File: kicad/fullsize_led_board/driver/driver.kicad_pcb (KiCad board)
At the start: 2 copper layers, 0 parts

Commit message: fullsize led board: driver pcb outline and connectors placed
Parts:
- added C1: 100nF, Capacitor_THT:C_Disc_D4.7mm_W2.5mm_P5.00mm, F.Cu at (163.9, 71.9)
- added C2: 100nF, Capacitor_THT:C_Disc_D4.7mm_W2.5mm_P5.00mm, F.Cu at (163.9, 75.9)
- added C3: 100nF, Capacitor_THT:C_Disc_D4.7mm_W2.5mm_P5.00mm, F.Cu at (163.9, 80.0)
- added C4: 100nF, Capacitor_THT:C_Disc_D4.7mm_W2.5mm_P5.00mm, F.Cu at (163.9, 84.0)
- added C5: 100nF, Capacitor_THT:C_Disc_D4.7mm_W2.5mm_P5.00mm, F.Cu at (163.9, 88.1)
- added C6: 100nF, Capacitor_THT:C_Disc_D4.7mm_W2.5mm_P5.00mm, F.Cu at (163.9, 92.1)
- added C7: 100nF, Capacitor_THT:C_Disc_D4.7mm_W2.5mm_P5.00mm, F.Cu at (163.9, 96.2)
- added C8: 100nF, Capacitor_THT:C_Disc_D4.7mm_W2.5mm_P5.00mm, F.Cu at (163.9, 100.2)
- added J1: ~, Connector_PinHeader_2.54mm:PinHeader_1x02_P2.54mm_Horizontal, F.Cu at (249.9, 123.7)
- added J2: ~, Connector_BarrelJack:BarrelJack_Horizontal, F.Cu at (246.0, 137.0)
- added J3: ~, Connector_PinHeader_2.54mm:PinHeader_2x05_P2.54mm_Horizontal, F.Cu at (247.3, 108.5)
- added J4: Anodes Header, Connector_PinSocket_2.54mm:PinSocket_1x24_P2.54mm_Vertical, F.Cu at (257.0, 40.0)
- added J5: Cathodes Header, Connector_PinSocket_2.54mm:PinSocket_1x32_P2.54mm_Vertical, F.Cu at (103.9, 157.0)
- added Q1: SQ2351CES, Package_TO_SOT_SMD:SOT-23-3, F.Cu at (173.1, 72.2)
- added Q10: SQ2351CES, Package_TO_SOT_SMD:SOT-23-3, F.Cu at (178.2, 81.5)
- added Q11: SQ2351CES, Package_TO_SOT_SMD:SOT-23-3, F.Cu at (178.2, 86.1)
- added Q12: SQ2351CES, Package_TO_SOT_SMD:SOT-23-3, F.Cu at (178.2, 90.8)
- added Q13: SQ2351CES, Package_TO_SOT_SMD:SOT-23-3, F.Cu at (178.2, 95.4)
- added Q14: SQ2351CES, Package_TO_SOT_SMD:SOT-23-3, F.Cu at (178.2, 100.0)
- added Q15: SQ2351CES, Package_TO_SOT_SMD:SOT-23-3, F.Cu at (183.4, 72.2)
- added Q16: SQ2351CES, Package_TO_SOT_SMD:SOT-23-3, F.Cu at (183.4, 76.9)
- added Q17: SQ2351CES, Package_TO_SOT_SMD:SOT-23-3, F.Cu at (183.4, 81.5)
- added Q18: SQ2351CES, Package_TO_SOT_SMD:SOT-23-3, F.Cu at (183.4, 86.1)
- added Q19: SQ2351CES, Package_TO_SOT_SMD:SOT-23-3, F.Cu at (183.4, 90.8)
- added Q2: SQ2351CES, Package_TO_SOT_SMD:SOT-23-3, F.Cu at (173.1, 76.9)
- added Q20: SQ2351CES, Package_TO_SOT_SMD:SOT-23-3, F.Cu at (183.4, 95.4)
- added Q21: SQ2351CES, Package_TO_SOT_SMD:SOT-23-3, F.Cu at (183.4, 100.0)
- added Q22: SQ2351CES, Package_TO_SOT_SMD:SOT-23-3, F.Cu at (188.5, 72.2)
- added Q23: SQ2351CES, Package_TO_SOT_SMD:SOT-23-3, F.Cu at (188.5, 76.9)
- added Q24: SQ2351CES, Package_TO_SOT_SMD:SOT-23-3, F.Cu at (188.5, 81.5)
- added Q3: SQ2351CES, Package_TO_SOT_SMD:SOT-23-3, F.Cu at (173.1, 81.5)
- added Q4: SQ2351CES, Package_TO_SOT_SMD:SOT-23-3, F.Cu at (173.1, 86.1)
- added Q5: SQ2351CES, Package_TO_SOT_SMD:SOT-23-3, F.Cu at (173.1, 90.8)
- added Q6: SQ2351CES, Package_TO_SOT_SMD:SOT-23-3, F.Cu at (173.1, 95.4)
- added Q7: SQ2351CES, Package_TO_SOT_SMD:SOT-23-3, F.Cu at (173.1, 100.0)
- added Q8: SQ2351CES, Package_TO_SOT_SMD:SOT-23-3, F.Cu at (178.2, 72.2)
- added Q9: SQ2351CES, Package_TO_SOT_SMD:SOT-23-3, F.Cu at (178.2, 76.9)
- added R1: R, Resistor_THT:R_Axial_DIN0207_L6.3mm_D2.5mm_P7.62mm_Horizontal, F.Cu at (110.1, 71.9)
- added R10: 150R, Resistor_THT:R_Axial_DIN0207_L6.3mm_D2.5mm_P7.62mm_Horizontal, F.Cu at (110.1, 108.3)
- added R11: R, Resistor_THT:R_Axial_DIN0207_L6.3mm_D2.5mm_P7.62mm_Horizontal, F.Cu at (110.1, 112.4)
- added R12: 150R, Resistor_THT:R_Axial_DIN0207_L6.3mm_D2.5mm_P7.62mm_Horizontal, F.Cu at (120.8, 71.9)
- added R13: R, Resistor_THT:R_Axial_DIN0207_L6.3mm_D2.5mm_P7.62mm_Horizontal, F.Cu at (120.8, 75.9)
- added R14: 150R, Resistor_THT:R_Axial_DIN0207_L6.3mm_D2.5mm_P7.62mm_Horizontal, F.Cu at (120.8, 80.0)
- added R15: R, Resistor_THT:R_Axial_DIN0207_L6.3mm_D2.5mm_P7.62mm_Horizontal, F.Cu at (120.8, 84.0)
- added R16: 150R, Resistor_THT:R_Axial_DIN0207_L6.3mm_D2.5mm_P7.62mm_Horizontal, F.Cu at (120.8, 88.1)
- added R17: R, Resistor_THT:R_Axial_DIN0207_L6.3mm_D2.5mm_P7.62mm_Horizontal, F.Cu at (120.8, 92.1)
- added R18: 150R, Resistor_THT:R_Axial_DIN0207_L6.3mm_D2.5mm_P7.62mm_Horizontal, F.Cu at (120.8, 96.2)
- added R19: R, Resistor_THT:R_Axial_DIN0207_L6.3mm_D2.5mm_P7.62mm_Horizontal, F.Cu at (120.8, 100.2)
- added R2: R, Resistor_THT:R_Axial_DIN0207_L6.3mm_D2.5mm_P7.62mm_Horizontal, F.Cu at (110.1, 75.9)
- added R20: 150R, Resistor_THT:R_Axial_DIN0207_L6.3mm_D2.5mm_P7.62mm_Horizontal, F.Cu at (120.8, 104.3)
- added R21: R, Resistor_THT:R_Axial_DIN0207_L6.3mm_D2.5mm_P7.62mm_Horizontal, F.Cu at (120.8, 108.3)
- added R22: 150R, Resistor_THT:R_Axial_DIN0207_L6.3mm_D2.5mm_P7.62mm_Horizontal, F.Cu at (120.8, 112.4)
- added R23: R, Resistor_THT:R_Axial_DIN0207_L6.3mm_D2.5mm_P7.62mm_Horizontal, F.Cu at (131.6, 71.9)
- added R24: 150R, Resistor_THT:R_Axial_DIN0207_L6.3mm_D2.5mm_P7.62mm_Horizontal, F.Cu at (131.6, 75.9)
- added R25: R, Resistor_THT:R_Axial_DIN0207_L6.3mm_D2.5mm_P7.62mm_Horizontal, F.Cu at (131.6, 80.0)
- added R26: 150R, Resistor_THT:R_Axial_DIN0207_L6.3mm_D2.5mm_P7.62mm_Horizontal, F.Cu at (131.6, 84.0)
- added R27: R, Resistor_THT:R_Axial_DIN0207_L6.3mm_D2.5mm_P7.62mm_Horizontal, F.Cu at (131.6, 88.1)
- added R28: 150R, Resistor_THT:R_Axial_DIN0207_L6.3mm_D2.5mm_P7.62mm_Horizontal, F.Cu at (131.6, 92.1)
- added R29: R, Resistor_THT:R_Axial_DIN0207_L6.3mm_D2.5mm_P7.62mm_Horizontal, F.Cu at (131.6, 96.2)
- added R3: R, Resistor_THT:R_Axial_DIN0207_L6.3mm_D2.5mm_P7.62mm_Horizontal, F.Cu at (110.1, 80.0)
- added R30: 150R, Resistor_THT:R_Axial_DIN0207_L6.3mm_D2.5mm_P7.62mm_Horizontal, F.Cu at (131.6, 100.2)
- added R31: R, Resistor_THT:R_Axial_DIN0207_L6.3mm_D2.5mm_P7.62mm_Horizontal, F.Cu at (131.6, 104.3)
- added R32: 150R, Resistor_THT:R_Axial_DIN0207_L6.3mm_D2.5mm_P7.62mm_Horizontal, F.Cu at (131.6, 108.3)
- added R33: R, Resistor_THT:R_Axial_DIN0207_L6.3mm_D2.5mm_P7.62mm_Horizontal, F.Cu at (131.6, 112.4)
- added R34: 150R, Resistor_THT:R_Axial_DIN0207_L6.3mm_D2.5mm_P7.62mm_Horizontal, F.Cu at (142.4, 71.9)
- added R35: R, Resistor_THT:R_Axial_DIN0207_L6.3mm_D2.5mm_P7.62mm_Horizontal, F.Cu at (142.4, 75.9)
- added R36: 150R, Resistor_THT:R_Axial_DIN0207_L6.3mm_D2.5mm_P7.62mm_Horizontal, F.Cu at (142.4, 80.0)
- added R37: R, Resistor_THT:R_Axial_DIN0207_L6.3mm_D2.5mm_P7.62mm_Horizontal, F.Cu at (142.4, 84.0)
- added R38: 150R, Resistor_THT:R_Axial_DIN0207_L6.3mm_D2.5mm_P7.62mm_Horizontal, F.Cu at (142.4, 88.1)
- added R39: R, Resistor_THT:R_Axial_DIN0207_L6.3mm_D2.5mm_P7.62mm_Horizontal, F.Cu at (142.4, 92.1)
- added R4: R, Resistor_THT:R_Axial_DIN0207_L6.3mm_D2.5mm_P7.62mm_Horizontal, F.Cu at (110.1, 84.0)
- added R40: 150R, Resistor_THT:R_Axial_DIN0207_L6.3mm_D2.5mm_P7.62mm_Horizontal, F.Cu at (142.4, 96.2)
- added R41: R, Resistor_THT:R_Axial_DIN0207_L6.3mm_D2.5mm_P7.62mm_Horizontal, F.Cu at (142.4, 100.2)
- added R42: 150R, Resistor_THT:R_Axial_DIN0207_L6.3mm_D2.5mm_P7.62mm_Horizontal, F.Cu at (142.4, 104.3)
- added R43: R, Resistor_THT:R_Axial_DIN0207_L6.3mm_D2.5mm_P7.62mm_Horizontal, F.Cu at (142.4, 108.3)
- added R44: 150R, Resistor_THT:R_Axial_DIN0207_L6.3mm_D2.5mm_P7.62mm_Horizontal, F.Cu at (142.4, 112.4)
- added R45: R, Resistor_THT:R_Axial_DIN0207_L6.3mm_D2.5mm_P7.62mm_Horizontal, F.Cu at (153.1, 71.9)
- added R46: 150R, Resistor_THT:R_Axial_DIN0207_L6.3mm_D2.5mm_P7.62mm_Horizontal, F.Cu at (153.1, 75.9)
- added R47: R, Resistor_THT:R_Axial_DIN0207_L6.3mm_D2.5mm_P7.62mm_Horizontal, F.Cu at (153.1, 80.0)
- added R48: 150R, Resistor_THT:R_Axial_DIN0207_L6.3mm_D2.5mm_P7.62mm_Horizontal, F.Cu at (153.1, 84.0)
- added R49: R, Resistor_THT:R_Axial_DIN0207_L6.3mm_D2.5mm_P7.62mm_Horizontal, F.Cu at (153.1, 88.1)
- added R5: R, Resistor_THT:R_Axial_DIN0207_L6.3mm_D2.5mm_P7.62mm_Horizontal, F.Cu at (110.1, 88.1)
- added R50: 150R, Resistor_THT:R_Axial_DIN0207_L6.3mm_D2.5mm_P7.62mm_Horizontal, F.Cu at (153.1, 92.1)
- added R51: R, Resistor_THT:R_Axial_DIN0207_L6.3mm_D2.5mm_P7.62mm_Horizontal, F.Cu at (153.1, 96.2)
- added R52: 150R, Resistor_THT:R_Axial_DIN0207_L6.3mm_D2.5mm_P7.62mm_Horizontal, F.Cu at (153.1, 100.2)
- added R53: R, Resistor_THT:R_Axial_DIN0207_L6.3mm_D2.5mm_P7.62mm_Horizontal, F.Cu at (153.1, 104.3)
- added R54: 150R, Resistor_THT:R_Axial_DIN0207_L6.3mm_D2.5mm_P7.62mm_Horizontal, F.Cu at (153.1, 108.3)
- added R55: R, Resistor_THT:R_Axial_DIN0207_L6.3mm_D2.5mm_P7.62mm_Horizontal, F.Cu at (103.9, 149.5)
- added R56: R, Resistor_THT:R_Axial_DIN0207_L6.3mm_D2.5mm_P7.62mm_Horizontal, F.Cu at (106.9, 149.5)
- added R57: R, Resistor_THT:R_Axial_DIN0207_L6.3mm_D2.5mm_P7.62mm_Horizontal, F.Cu at (109.9, 149.5)
- added R58: R, Resistor_THT:R_Axial_DIN0207_L6.3mm_D2.5mm_P7.62mm_Horizontal, F.Cu at (112.9, 149.5)
- added R59: R, Resistor_THT:R_Axial_DIN0207_L6.3mm_D2.5mm_P7.62mm_Horizontal, F.Cu at (115.9, 149.5)
- added R6: R, Resistor_THT:R_Axial_DIN0207_L6.3mm_D2.5mm_P7.62mm_Horizontal, F.Cu at (110.1, 92.1)
- added R60: R, Resistor_THT:R_Axial_DIN0207_L6.3mm_D2.5mm_P7.62mm_Horizontal, F.Cu at (118.9, 149.5)
- added R61: R, Resistor_THT:R_Axial_DIN0207_L6.3mm_D2.5mm_P7.62mm_Horizontal, F.Cu at (121.9, 149.5)
- added R62: R, Resistor_THT:R_Axial_DIN0207_L6.3mm_D2.5mm_P7.62mm_Horizontal, F.Cu at (124.9, 149.5)
- added R63: R, Resistor_THT:R_Axial_DIN0207_L6.3mm_D2.5mm_P7.62mm_Horizontal, F.Cu at (127.9, 149.5)
- added R64: R, Resistor_THT:R_Axial_DIN0207_L6.3mm_D2.5mm_P7.62mm_Horizontal, F.Cu at (130.9, 149.5)
- added R65: R, Resistor_THT:R_Axial_DIN0207_L6.3mm_D2.5mm_P7.62mm_Horizontal, F.Cu at (133.9, 149.5)
- added R66: R, Resistor_THT:R_Axial_DIN0207_L6.3mm_D2.5mm_P7.62mm_Horizontal, F.Cu at (136.9, 149.5)
- added R67: R, Resistor_THT:R_Axial_DIN0207_L6.3mm_D2.5mm_P7.62mm_Horizontal, F.Cu at (139.9, 149.5)
- added R68: R, Resistor_THT:R_Axial_DIN0207_L6.3mm_D2.5mm_P7.62mm_Horizontal, F.Cu at (142.9, 149.5)
- added R69: R, Resistor_THT:R_Axial_DIN0207_L6.3mm_D2.5mm_P7.62mm_Horizontal, F.Cu at (145.9, 149.5)
- added R7: R, Resistor_THT:R_Axial_DIN0207_L6.3mm_D2.5mm_P7.62mm_Horizontal, F.Cu at (110.1, 96.2)
- added R70: R, Resistor_THT:R_Axial_DIN0207_L6.3mm_D2.5mm_P7.62mm_Horizontal, F.Cu at (148.9, 149.5)
- added R71: R, Resistor_THT:R_Axial_DIN0207_L6.3mm_D2.5mm_P7.62mm_Horizontal, F.Cu at (151.9, 149.5)
- added R72: R, Resistor_THT:R_Axial_DIN0207_L6.3mm_D2.5mm_P7.62mm_Horizontal, F.Cu at (154.9, 149.5)
- added R73: R, Resistor_THT:R_Axial_DIN0207_L6.3mm_D2.5mm_P7.62mm_Horizontal, F.Cu at (157.9, 149.5)
- added R74: R, Resistor_THT:R_Axial_DIN0207_L6.3mm_D2.5mm_P7.62mm_Horizontal, F.Cu at (160.9, 149.5)
- added R75: R, Resistor_THT:R_Axial_DIN0207_L6.3mm_D2.5mm_P7.62mm_Horizontal, F.Cu at (163.9, 149.5)
- added R76: R, Resistor_THT:R_Axial_DIN0207_L6.3mm_D2.5mm_P7.62mm_Horizontal, F.Cu at (166.9, 149.5)
- added R77: R, Resistor_THT:R_Axial_DIN0207_L6.3mm_D2.5mm_P7.62mm_Horizontal, F.Cu at (169.9, 149.5)
- added R78: R, Resistor_THT:R_Axial_DIN0207_L6.3mm_D2.5mm_P7.62mm_Horizontal, F.Cu at (172.9, 149.5)
- added R79: R, Resistor_THT:R_Axial_DIN0207_L6.3mm_D2.5mm_P7.62mm_Horizontal, F.Cu at (175.9, 149.5)
- added R8: 150R, Resistor_THT:R_Axial_DIN0207_L6.3mm_D2.5mm_P7.62mm_Horizontal, F.Cu at (110.1, 100.2)
- added R80: R, Resistor_THT:R_Axial_DIN0207_L6.3mm_D2.5mm_P7.62mm_Horizontal, F.Cu at (178.9, 149.5)
- added R81: R, Resistor_THT:R_Axial_DIN0207_L6.3mm_D2.5mm_P7.62mm_Horizontal, F.Cu at (181.9, 149.5)
- added R82: R, Resistor_THT:R_Axial_DIN0207_L6.3mm_D2.5mm_P7.62mm_Horizontal, F.Cu at (184.9, 149.5)
- added R83: R, Resistor_THT:R_Axial_DIN0207_L6.3mm_D2.5mm_P7.62mm_Horizontal, F.Cu at (187.9, 149.5)
- added R84: R, Resistor_THT:R_Axial_DIN0207_L6.3mm_D2.5mm_P7.62mm_Horizontal, F.Cu at (190.9, 149.5)
- added R85: R, Resistor_THT:R_Axial_DIN0207_L6.3mm_D2.5mm_P7.62mm_Horizontal, F.Cu at (193.9, 149.5)
- added R86: R, Resistor_THT:R_Axial_DIN0207_L6.3mm_D2.5mm_P7.62mm_Horizontal, F.Cu at (196.9, 149.5)
- added R9: R, Resistor_THT:R_Axial_DIN0207_L6.3mm_D2.5mm_P7.62mm_Horizontal, F.Cu at (110.1, 104.3)
- added U1: 74HCT541, Package_DIP:DIP-20_W7.62mm, F.Cu at (110.1, 44.9)
- added U2: 74HCT595, Package_SO:SOIC-16_3.9x9.9mm_P1.27mm, F.Cu at (167.0, 48.7)
- added U3: 74HCT595, Package_SO:SOIC-16_3.9x9.9mm_P1.27mm, F.Cu at (175.4, 48.7)
- added U4: 74HCT595, Package_SO:SOIC-16_3.9x9.9mm_P1.27mm, F.Cu at (183.9, 48.7)
- added U5: TPIC6B595N, Package_DIP:DIP-20_W7.62mm, F.Cu at (121.0, 44.9)
- added U6: TPIC6B595N, Package_DIP:DIP-20_W7.62mm, F.Cu at (131.8, 44.9)
- added U7: TPIC6B595N, Package_DIP:DIP-20_W7.62mm, F.Cu at (142.7, 44.9)
- added U8: TPIC6B595N, Package_DIP:DIP-20_W7.62mm, F.Cu at (153.5, 44.9)
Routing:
- net Net-(J1-Pin_2): track 0.00 -> 6.40 mm
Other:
- board outline added: 163.5 x 127.5 mm
- rule pad_to_mask_clearance: 0 -> 0.038

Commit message: fullsize led board: anode components placed and partially wired
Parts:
- Q10, Q12, Q14, Q16, Q18, Q2, Q20, Q22, Q24, Q4, Q6, Q8, U1, U2, U3, U4: moved to B.Cu
- R1, R11, R13, R15, R17, R19, R2, R21, R23, R25, R27, R29, R3, R31, R33, R35, R37, R39, R4, R41, R43, R45, R47, R49, R5, R51, R53, R6, R7, R9: value R -> 10K
- moved C4 156.0 mm to (313.0, 38.0), turned to -90 degrees
- moved C3 146.7 mm to (304.5, 38.0), turned to -90 degrees
- moved R11 144.3 mm to (235.8, 41.7), turned to 180 degrees
- moved R9 141.8 mm to (235.8, 38.7), turned to 180 degrees
- moved R7 139.5 mm to (235.8, 35.7), turned to 180 degrees
- moved C2 138.6 mm to (295.0, 31.0), turned to -90 degrees
- moved C5 138.5 mm to (25.5, 84.5)
- moved R10 134.7 mm to (225.3, 38.7), turned to 180 degrees
- moved R8 132.1 mm to (225.3, 35.7), turned to 180 degrees
- moved R6 131.6 mm to (232.0, 141.6), turned to 90 degrees
- moved R5 130.4 mm to (229.0, 141.6), turned to 90 degrees
- moved R4 129.5 mm to (226.0, 141.6), turned to 90 degrees
- moved R3 128.7 mm to (223.0, 141.6), turned to 90 degrees
- moved C6 128.6 mm to (35.5, 84.5)
- moved R2 128.1 mm to (220.0, 141.6), turned to 90 degrees
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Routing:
- net +5V: track 0.00 -> 263.0 mm, vias 0 -> 12
- net Net-(Q2-G): track 0.00 -> 21.0 mm, vias 0 -> 1
- net Net-(Q23-G): track 0.00 -> 20.6 mm
- net Net-(Q4-G): track 0.00 -> 20.5 mm, vias 0 -> 1
- net Net-(Q3-G): track 0.00 -> 20.0 mm
- net Net-(Q10-G): track 0.00 -> 19.7 mm, vias 0 -> 1
- net Net-(Q24-G): track 0.00 -> 19.6 mm, vias 0 -> 1
- net Net-(Q5-G): track 0.00 -> 19.5 mm
- net Net-(Q1-G): track 0.00 -> 19.5 mm
- net Net-(Q21-G): track 0.00 -> 19.4 mm
- net Net-(Q6-G): track 0.00 -> 19.3 mm, vias 0 -> 1
- net Net-(Q22-G): track 0.00 -> 19.2 mm, vias 0 -> 1
- net Net-(Q19-G): track 0.00 -> 19.1 mm
- net Net-(Q8-G): track 0.00 -> 19.0 mm, vias 0 -> 1
- net Net-(Q20-G): track 0.00 -> 18.8 mm, vias 0 -> 1
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- added copper zone on B.Cu, net GND

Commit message: fullsize led board: placed buffer and its pullups
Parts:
- C1: moved to B.Cu
- moved C1 162.0 mm to (206.0, 111.5), turned to 0 degrees
- moved C4 127.0 mm to (198.0, 92.0)
- moved C3 112.3 mm to (197.0, 70.5)
- moved C2 94.5 mm to (201.0, 40.5)
- moved R1 16.0 mm to (230.8, 133.5), turned to 180 degrees
- moved R2 12.0 mm to (230.8, 136.5), turned to 180 degrees
- moved R3 8.09 mm to (230.8, 139.5), turned to 180 degrees
- moved R6 6.98 mm to (230.8, 148.5), turned to 180 degrees
- moved R4 4.89 mm to (230.8, 142.5), turned to 180 degrees
- moved U1 4.40 mm to (212.3, 114.6)
- moved R5 4.28 mm to (230.8, 145.5), turned to 180 degrees
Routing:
- net RowData: track 0.00 -> 80.2 mm
- net ShiftRowData: track 0.00 -> 75.7 mm
- net RowStrobe: track 0.00 -> 74.8 mm
- net ShiftRowStrobe: track 0.00 -> 74.1 mm
- net ApplyRowAndStrobe: track 0.00 -> 71.1 mm
- net ~{OutputEnable}: track 0.00 -> 58.0 mm, vias 0 -> 1
- net +5V: track 263.0 -> 298.2 mm

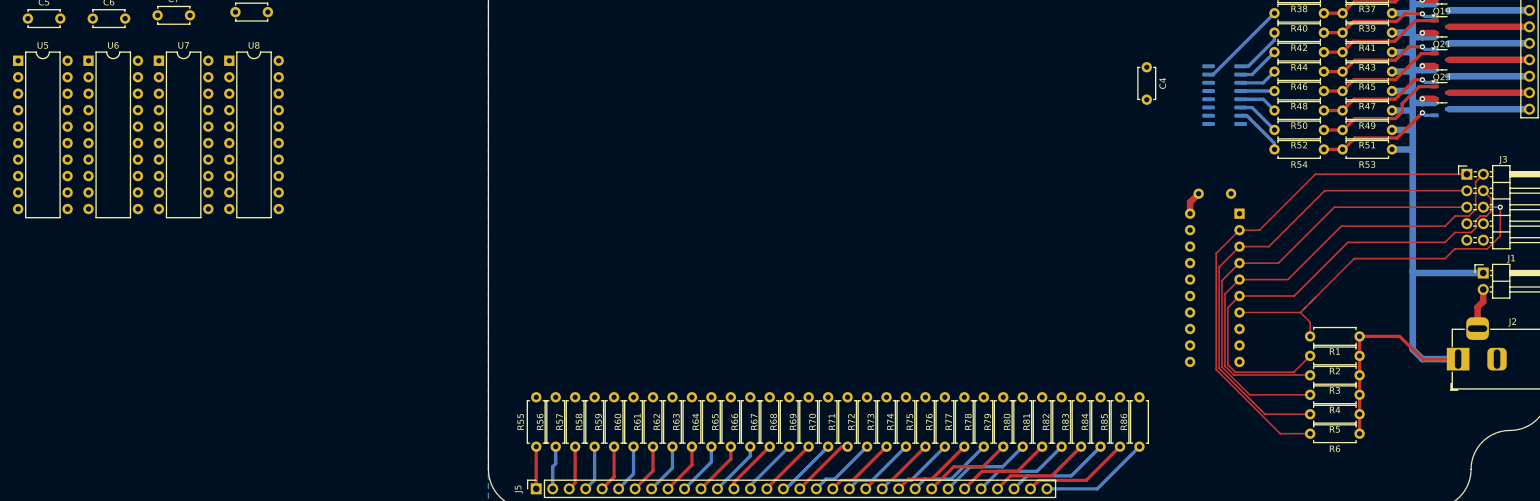
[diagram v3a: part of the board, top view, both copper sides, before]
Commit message: fullsize led board: placed and mostly routed row data shift registers
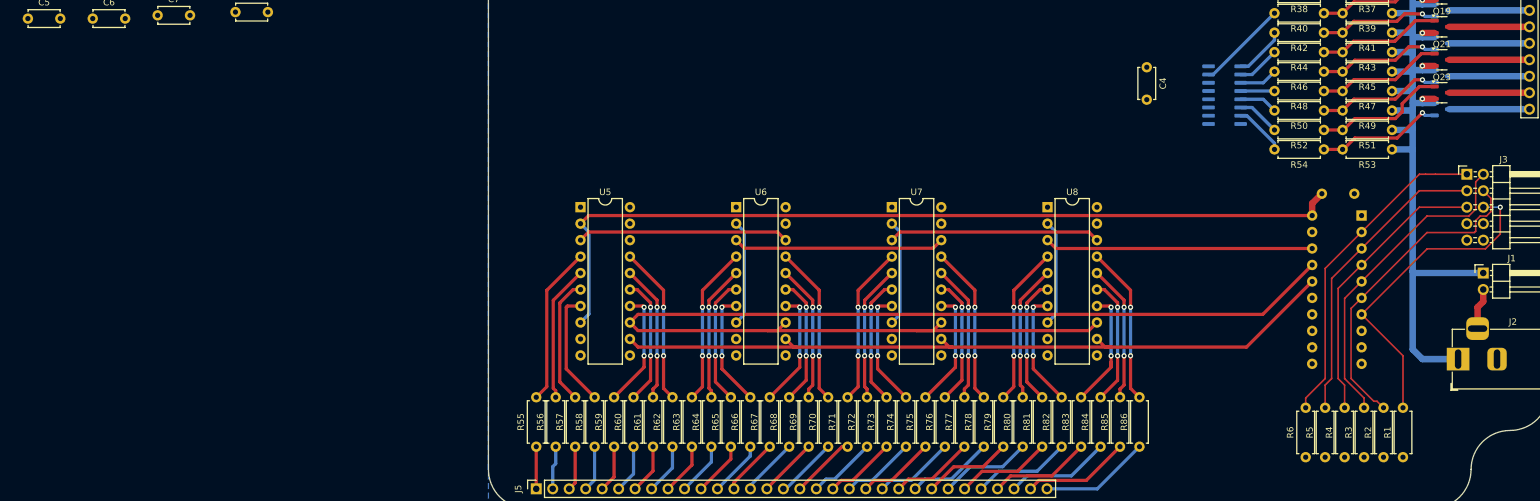
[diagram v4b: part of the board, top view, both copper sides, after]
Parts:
- moved U8 128.2 mm to (182.7, 113.6)
- moved U7 115.2 mm to (158.7, 113.6)
- moved U6 102.4 mm to (134.7, 113.6)
- moved U5 89.6 mm to (110.7, 113.6)
- moved R1 19.8 mm to (237.5, 152.1), turned to 90 degrees
- moved C1 19.0 mm to (225.0, 111.5)
- moved U1 18.8 mm to (231.1, 114.9)
- moved R2 16.0 mm to (234.5, 152.1), turned to 90 degrees
- moved R3 12.6 mm to (231.5, 152.1), turned to 90 degrees
- moved R4 9.89 mm to (228.5, 152.1), turned to 90 degrees
- moved R6 9.06 mm to (222.5, 152.1), turned to 90 degrees
- moved R5 8.49 mm to (225.5, 152.1), turned to 90 degrees
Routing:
- net /ShiftRowData': track 0.00 -> 189.6 mm
- net +5V: track 298.2 -> 445.4 mm
- net /ApplyRowAndStrobe': track 0.00 -> 117.0 mm
- net /RowData': track 0.00 -> 41.7 mm
- net Net-(U7-SER_IN): track 0.00 -> 32.7 mm
- net Net-(U6-SER_IN): track 0.00 -> 32.7 mm
- net Net-(U5-SER_IN): track 0.00 -> 32.7 mm
- net RowData: track 80.2 -> 50.6 mm
- net ShiftRowData: track 75.7 -> 46.8 mm
- net ApplyRowAndStrobe: track 71.1 -> 43.8 mm
- net RowStrobe: track 74.8 -> 49.9 mm
- net /Cathodes8: track 0.00 -> 24.5 mm, vias 0 -> 2
- net /Cathodes0: track 0.00 -> 24.5 mm
- net /Cathodes24: track 0.00 -> 24.5 mm, vias 0 -> 2
- net /Cathodes16: track 0.00 -> 24.5 mm, vias 0 -> 2
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
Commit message: fullsize led board: rearranged high-side resistors to eliminate voltage divier
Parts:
- moved C8 124.3 mm to (179.8, 106.2)
- moved C7 114.8 mm to (158.2, 105.8)
- moved C6 99.9 mm to (133.8, 102.5)
- moved C5 88.3 mm to (112.5, 99.8)
- moved R11 7.62 mm to (228.2, 41.7), turned to 0 degrees
- moved R13 7.62 mm to (228.2, 44.7), turned to 0 degrees
- moved R15 7.62 mm to (228.2, 47.7), turned to 0 degrees
- moved R17 7.62 mm to (228.2, 50.7), turned to 0 degrees
- moved R19 7.62 mm to (228.2, 53.7), turned to 0 degrees
- moved R21 7.62 mm to (228.2, 56.7), turned to 0 degrees
- moved R23 7.62 mm to (228.2, 59.7), turned to 0 degrees
- moved R25 7.62 mm to (228.2, 62.7), turned to 0 degrees
- moved R27 7.62 mm to (228.2, 65.7), turned to 0 degrees
- moved R29 7.62 mm to (228.2, 68.7), turned to 0 degrees
- moved R31 7.62 mm to (228.2, 71.7), turned to 0 degrees
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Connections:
- J3 pad 1: RowData -> ApplyRowAndStrobe
- J3 pad 2: RowStrobe -> ApplyRowAndStrobe
- J3 pad 3: ShiftRowData -> ApplyRowAndStrobe
- J3 pad 6: ~{OutputEnable} -> ApplyRowAndStrobe
- Q17 pad 2: +5V -> unconnected-(Q17-S-Pad2)
- Q17 pad 3: /Anodes16 -> unconnected-(Q17-D-Pad3)
- Q18 pad 2: +5V -> unconnected-(Q18-S-Pad2)
- Q18 pad 3: /Anodes17 -> unconnected-(Q18-D-Pad3)
- Q19 pad 2: +5V -> unconnected-(Q19-S-Pad2)
- Q19 pad 3: /Anodes18 -> unconnected-(Q19-D-Pad3)
- Q20 pad 2: +5V -> unconnected-(Q20-S-Pad2)
- Q20 pad 3: /Anodes19 -> unconnected-(Q20-D-Pad3)
- Q21 pad 2: +5V -> unconnected-(Q21-S-Pad2)
- Q21 pad 3: /Anodes20 -> unconnected-(Q21-D-Pad3)
- Q22 pad 2: +5V -> unconnected-(Q22-S-Pad2)
- Q22 pad 3: /Anodes21 -> unconnected-(Q22-D-Pad3)
- Q23 pad 2: +5V -> unconnected-(Q23-S-Pad2)
- Q23 pad 3: /Anodes22 -> unconnected-(Q23-D-Pad3)
- Q24 pad 2: +5V -> unconnected-(Q24-S-Pad2)
- Q24 pad 3: /Anodes23 -> unconnected-(Q24-D-Pad3)
- R1 pad 1: +5V -> ApplyRowAndStrobe
- R1 pad 2: ~{OutputEnable} -> +5V
- R11 pad 1: +5V -> /Gates2
- R11 pad 2: Net-(Q3-G) -> +5V
- R13 pad 1: +5V -> /Gates3
- R13 pad 2: Net-(Q4-G) -> +5V
- R15 pad 1: +5V -> /Gates4
- R15 pad 2: Net-(Q5-G) -> +5V
- R17 pad 1: +5V -> /Gates5
- R17 pad 2: Net-(Q6-G) -> +5V
- R19 pad 1: +5V -> /Gates6
- R19 pad 2: Net-(Q7-G) -> +5V
- R21 pad 1: +5V -> /Gates7
- R21 pad 2: Net-(Q8-G) -> +5V
- R23 pad 1: +5V -> /Gates8
- R23 pad 2: Net-(Q9-G) -> +5V
- R25 pad 1: +5V -> /Gates9
- R25 pad 2: Net-(Q10-G) -> +5V
- R27 pad 1: +5V -> /Gates10
- R27 pad 2: Net-(Q11-G) -> +5V
- R29 pad 1: +5V -> /Gates11
- R29 pad 2: Net-(Q12-G) -> +5V
- R3 pad 1: +5V -> ApplyRowAndStrobe
- R3 pad 2: RowStrobe -> +5V
- R31 pad 1: +5V -> /Gates12
- R31 pad 2: Net-(Q13-G) -> +5V
- R33 pad 1: +5V -> /Gates13
- R33 pad 2: Net-(Q14-G) -> +5V
- R35 pad 1: +5V -> /Gates14
- R35 pad 2: Net-(Q15-G) -> +5V
- R37 pad 1: +5V -> /Gates15
- R37 pad 2: Net-(Q16-G) -> +5V
- R39 pad 1: +5V -> /Gates16
- R39 pad 2: Net-(Q17-G) -> +5V
- R4 pad 1: +5V -> ApplyRowAndStrobe
- R4 pad 2: ApplyRowAndStrobe -> +5V
- R41 pad 1: +5V -> /Gates17
- R41 pad 2: Net-(Q18-G) -> +5V
- R43 pad 1: +5V -> /Gates18
- R43 pad 2: Net-(Q19-G) -> +5V
- R45 pad 1: +5V -> /Gates19
- R45 pad 2: Net-(Q20-G) -> +5V
- R47 pad 1: +5V -> /Gates20
- R47 pad 2: Net-(Q21-G) -> +5V
- R49 pad 1: +5V -> /Gates21
- R49 pad 2: Net-(Q22-G) -> +5V
- R5 pad 1: +5V -> ApplyRowAndStrobe
- R5 pad 2: ShiftRowData -> +5V
- R51 pad 1: +5V -> /Gates22
- R51 pad 2: Net-(Q23-G) -> +5V
- R53 pad 1: +5V -> /Gates23
- R53 pad 2: Net-(Q24-G) -> +5V
- R6 pad 1: +5V -> ApplyRowAndStrobe
- R6 pad 2: RowData -> +5V
- R7 pad 1: +5V -> /Gates0
- R7 pad 2: Net-(Q1-G) -> +5V
- R9 pad 1: +5V -> /Gates1
- R9 pad 2: Net-(Q2-G) -> +5V
- U1 pad 2: RowData -> ApplyRowAndStrobe
- U1 pad 3: ShiftRowData -> ApplyRowAndStrobe
- U1 pad 5: RowStrobe -> ApplyRowAndStrobe
- U1 pad 7: ~{OutputEnable} -> ApplyRowAndStrobe
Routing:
- net (no net): track 0.00 -> 197.7 mm
- net /~{OutputEnable'}: track 0.00 -> 64.0 mm, vias 0 -> 3
- net /RowStrobe': track 0.00 -> 61.0 mm, vias 0 -> 1
- net /ShiftRowStrobe': track 0.00 -> 60.1 mm, vias 0 -> 3
- net /ApplyRowAndStrobe': track 117.0 -> 173.7 mm, vias 0 -> 3
- net RowData: track 50.6 -> 0.00 mm
- net ~{OutputEnable}: track 50.4 -> 0.00 mm, vias 1 -> 0
- net RowStrobe: track 49.9 -> 0.00 mm
- net ShiftRowData: track 46.8 -> 0.00 mm
- net Net-(U3-QH'): track 0.00 -> 21.3 mm, vias 0 -> 2
- net Net-(U2-QH'): track 0.00 -> 21.3 mm, vias 0 -> 2
- net /Gates8: track 14.1 -> 25.6 mm
- net /Gates22: track 6.65 -> 18.2 mm
- net /Gates16: track 14.1 -> 25.6 mm
- net /Gates14: track 6.65 -> 18.2 mm
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
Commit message: fullsize led board: routed pcb completely, silkscreen fix up next
Also some connections were fixed in the schematic.
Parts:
- moved C4 52.3 mm to (207.5, 41.5), turned to 90 degrees
- moved C2 49.4 mm to (207.5, 89.5), turned to 90 degrees
- moved C3 11.7 mm to (207.5, 65.5), turned to 90 degrees
- moved C5 10.8 mm to (112.0, 110.5)
- moved R1 8.85 mm to (235.0, 143.5), turned to -90 degrees
- moved R3 8.85 mm to (229.0, 143.5), turned to -90 degrees
- moved R4 8.85 mm to (226.0, 143.5), turned to -90 degrees
- moved R5 8.85 mm to (223.0, 143.5), turned to -90 degrees
- moved R6 8.85 mm to (220.0, 143.5), turned to -90 degrees
- moved C6 8.31 mm to (136.0, 110.5)
- moved C8 6.01 mm to (184.0, 110.5)
- moved C7 5.06 mm to (160.0, 110.5)
- moved R2 2.24 mm to (232.0, 151.1)
- moved U1 1.30 mm to (231.3, 113.6)
- moved C1 1.00 mm to (225.0, 110.5)
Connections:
- J3 pad 1: ApplyRowAndStrobe -> RowData
- J3 pad 2: ApplyRowAndStrobe -> RowStrobe
- J3 pad 3: ApplyRowAndStrobe -> ShiftRowData
- J3 pad 6: ApplyRowAndStrobe -> ~{OutputEnable}
- Q17 pad 2: unconnected-(Q17-S-Pad2) -> +5V
- Q17 pad 3: unconnected-(Q17-D-Pad3) -> /Anodes16
- Q18 pad 2: unconnected-(Q18-S-Pad2) -> +5V
- Q18 pad 3: unconnected-(Q18-D-Pad3) -> /Anodes17
- Q19 pad 2: unconnected-(Q19-S-Pad2) -> +5V
- Q19 pad 3: unconnected-(Q19-D-Pad3) -> /Anodes18
- Q20 pad 2: unconnected-(Q20-S-Pad2) -> +5V
- Q20 pad 3: unconnected-(Q20-D-Pad3) -> /Anodes19
- Q21 pad 2: unconnected-(Q21-S-Pad2) -> +5V
- Q21 pad 3: unconnected-(Q21-D-Pad3) -> /Anodes20
- Q22 pad 2: unconnected-(Q22-S-Pad2) -> +5V
- Q22 pad 3: unconnected-(Q22-D-Pad3) -> /Anodes21
- Q23 pad 2: unconnected-(Q23-S-Pad2) -> +5V
- Q23 pad 3: unconnected-(Q23-D-Pad3) -> /Anodes22
- Q24 pad 2: unconnected-(Q24-S-Pad2) -> +5V
- Q24 pad 3: unconnected-(Q24-D-Pad3) -> /Anodes23
- R1 pad 1: ApplyRowAndStrobe -> ~{OutputEnable}
- R3 pad 1: ApplyRowAndStrobe -> RowStrobe
- R5 pad 1: ApplyRowAndStrobe -> ShiftRowData
- R6 pad 1: ApplyRowAndStrobe -> RowData
- U1 pad 2: ApplyRowAndStrobe -> RowData
- U1 pad 3: ApplyRowAndStrobe -> ShiftRowData
- U1 pad 5: ApplyRowAndStrobe -> RowStrobe
- U1 pad 7: ApplyRowAndStrobe -> ~{OutputEnable}
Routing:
- net +5V: track 453.8 -> 662.7 mm, vias 12 -> 18
- net (no net): track 197.7 -> 0.00 mm
- net RowData: track 0.00 -> 51.3 mm
- net ~{OutputEnable}: track 0.00 -> 48.9 mm, vias 0 -> 1
- net RowStrobe: track 0.00 -> 48.5 mm
- net ShiftRowData: track 0.00 -> 47.5 mm
- net /ShiftRowStrobe': track 60.1 -> 106.6 mm, vias 3 -> 6
- net /ApplyRowAndStrobe': track 173.7 -> 215.7 mm, vias 3 -> 5
- net /~{OutputEnable'}: track 64.0 -> 95.7 mm, vias 3 -> 4
- net /RowStrobe': track 61.0 -> 87.2 mm, vias 1 -> 2
- net ShiftRowStrobe: track 49.6 -> 48.4 mm
- net Net-(Q10-G): track 19.7 -> 18.6 mm
- net /ShiftRowData': track 189.6 -> 190.3 mm
- net ApplyRowAndStrobe: track 43.6 -> 43.7 mm, vias 1 -> 0
